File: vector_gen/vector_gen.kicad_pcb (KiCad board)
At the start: 2 copper layers, 91.4 x 101.6 mm, 99 parts, among them J1 ARDUINO POWER 3.3V, J10 ARDUINO J1, J11 Conn_01x08, J2 ARDUINO J3 3.3V, J3 ARDUINO J2 3.3V, J4 Conn_01x02_Female, J5 ARDUINO J1 3.3V, J6 Conn_01x03, J7 ARDUINO POWER, J8 ARDUINO J3, J9 ARDUINO J2, Q1 2N3904, U1 MCP4922, U10 MCP4922, U11 MCP4922, U12 4019, U13 LM336, U14 74HC86, U16 74LS07, U17 74LS07, U19 MAX4544, U5 4066, U6 MCP6292, U8 TL072IP, U9 LM319

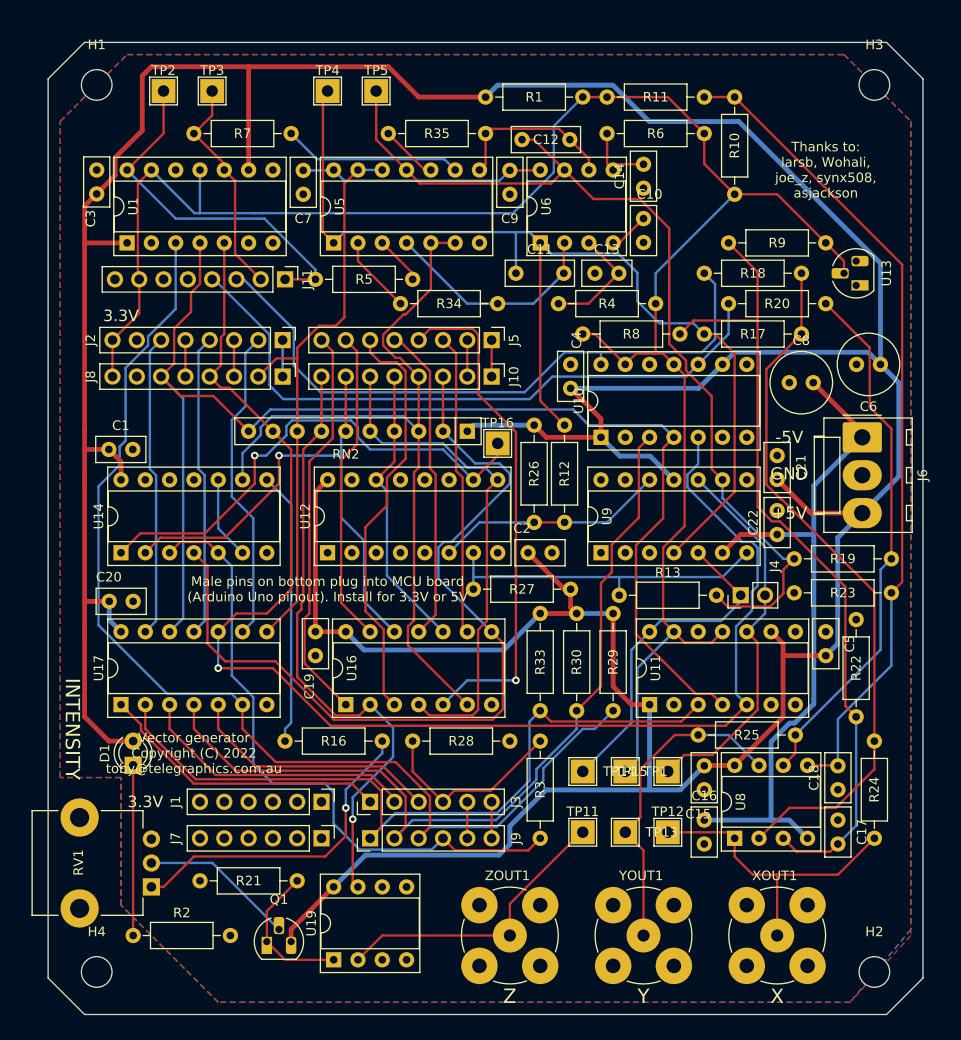
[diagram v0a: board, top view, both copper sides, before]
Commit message: Some important corrections. OSHpark candidate?
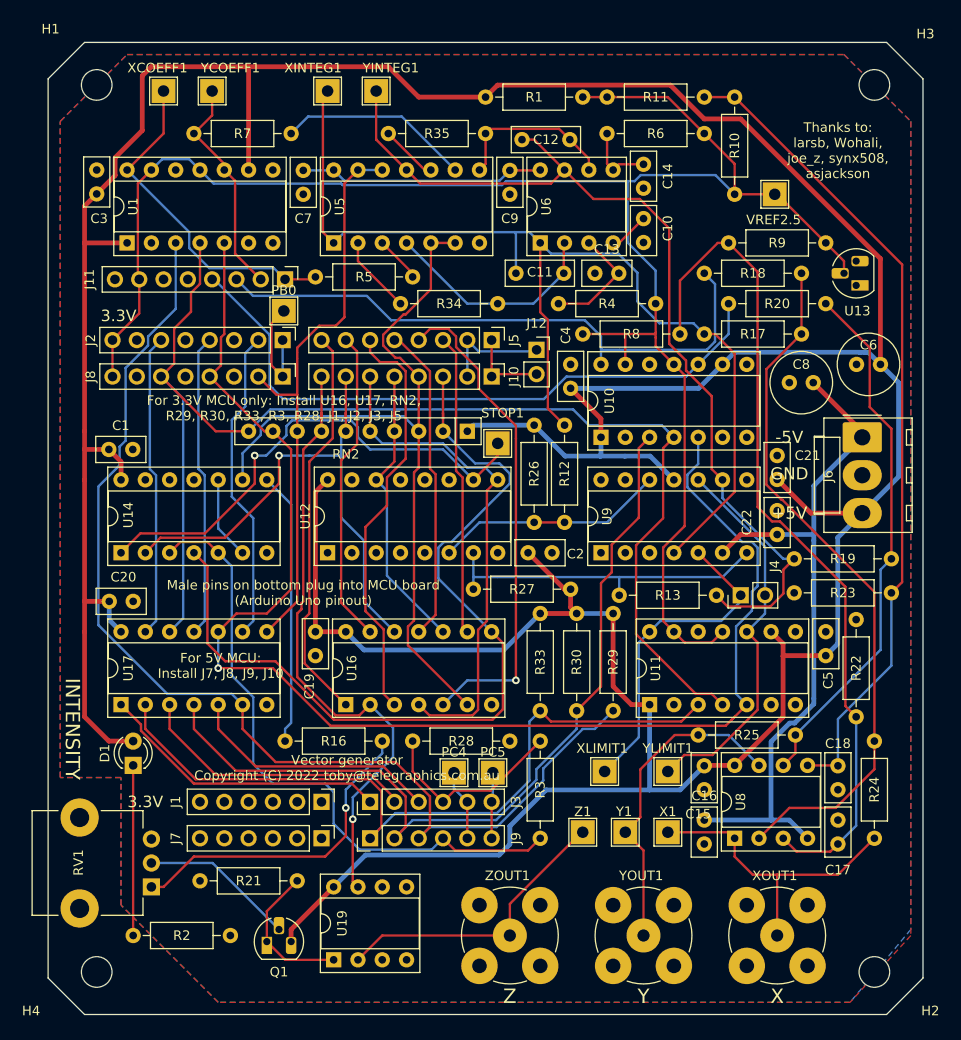
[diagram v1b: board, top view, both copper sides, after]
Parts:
- added J12: Conn_01x02, Connector_PinSocket_2.54mm:PinSocket_1x02_P2.54mm_Vertical, F.Cu at (-8.00, -24.4)
- added PB0: TestPoint, TestPoint:TestPoint_THTPad_2.5x2.5mm_Drill1.2mm, F.Cu at (-34.4, -28.4)
- added PC4: TestPoint, TestPoint:TestPoint_THTPad_2.5x2.5mm_Drill1.2mm, F.Cu at (-16.6, 19.8)
- added PC5: TestPoint, TestPoint:TestPoint_THTPad_2.5x2.5mm_Drill1.2mm, F.Cu at (-12.6, 19.8)
- moved VREF2.5 62.3 mm to (16.9, -40.6)
- moved XLIMIT1 2.29 mm to (-0.89, 19.7)
- moved R5 0.25 mm to (-21.0, -32.0)
- renumbered TP16 to STOP1, TP1 to VREF2.5, TP12 to X1, TP2 to XCOEFF1, TP4 to XINTEG1, TP14 to XLIMIT1, TP13 to Y1, TP3 to YCOEFF1, TP5 to YINTEG1, TP15 to YLIMIT1, TP11 to Z1
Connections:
- J1 pad 2: +3V3 -> GND
- J1 pad 3: Net-(J1-Pad3) -> GND
- J1 pad 4: GND -> Net-(J1-Pad4)
- J1 pad 5: GND -> +3V3
- J7 pad 2: Net-(J7-Pad2) -> GND
- J7 pad 3: Net-(J7-Pad3) -> GND
- J7 pad 4: GND -> Net-(J7-Pad4)
- J7 pad 5: GND -> Net-(J7-Pad5)
- J8 pad 1: Net-(J2-Pad1) -> Net-(J8-Pad1)
- J8 pad 3: Net-(J2-Pad3) -> Net-(J8-Pad3)
- J8 pad 5: Net-(J2-Pad5) -> Net-(J8-Pad5)
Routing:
- net Net-(J11-Pad7): track 204.7 -> 192.6 mm
- net Net-(J8-Pad1): track 0.00 -> 7.88 mm
- net Net-(J10-Pad2): track 3.81 -> 11.6 mm
- net Net-(J10-Pad1): track 3.81 -> 8.61 mm
- net Net-(J11-Pad3): track 68.0 -> 63.4 mm
- net Net-(J2-Pad5): track 3.81 -> 0.00 mm
- net Net-(J2-Pad3): track 3.81 -> 0.00 mm
- net Net-(J3-Pad5): track 3.81 -> 7.44 mm
- net Net-(C17-Pad2): track 84.9 -> 88.5 mm
- net Net-(J3-Pad6): track 3.81 -> 6.91 mm
- net Net-(J11-Pad1): track 38.0 -> 35.3 mm
- net +5V: track 467.7 -> 469.9 mm
- net Net-(J5-Pad4): track 53.4 -> 51.9 mm
- net Net-(R7-Pad1): track 18.7 -> 20.2 mm
- net Net-(J4-Pad1): track 35.3 -> 34.3 mm
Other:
- board text added: "For 3.3V MCU only: Install U16, U17, RN2, R29, R30, R33, R3, R28, J1, J2, J3, J5"
- board text added: "For 5V MCU: Install J7, J8, J9, J10"
- board text added: "Male pins on bottom plug into MCU board (Arduino Uno pinout)"
- board text removed: "Male pins on bottom plug into MCU board (Arduino Uno pinout). Install for 3.3V or 5V"

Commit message: New OSHPark manuf candidate.
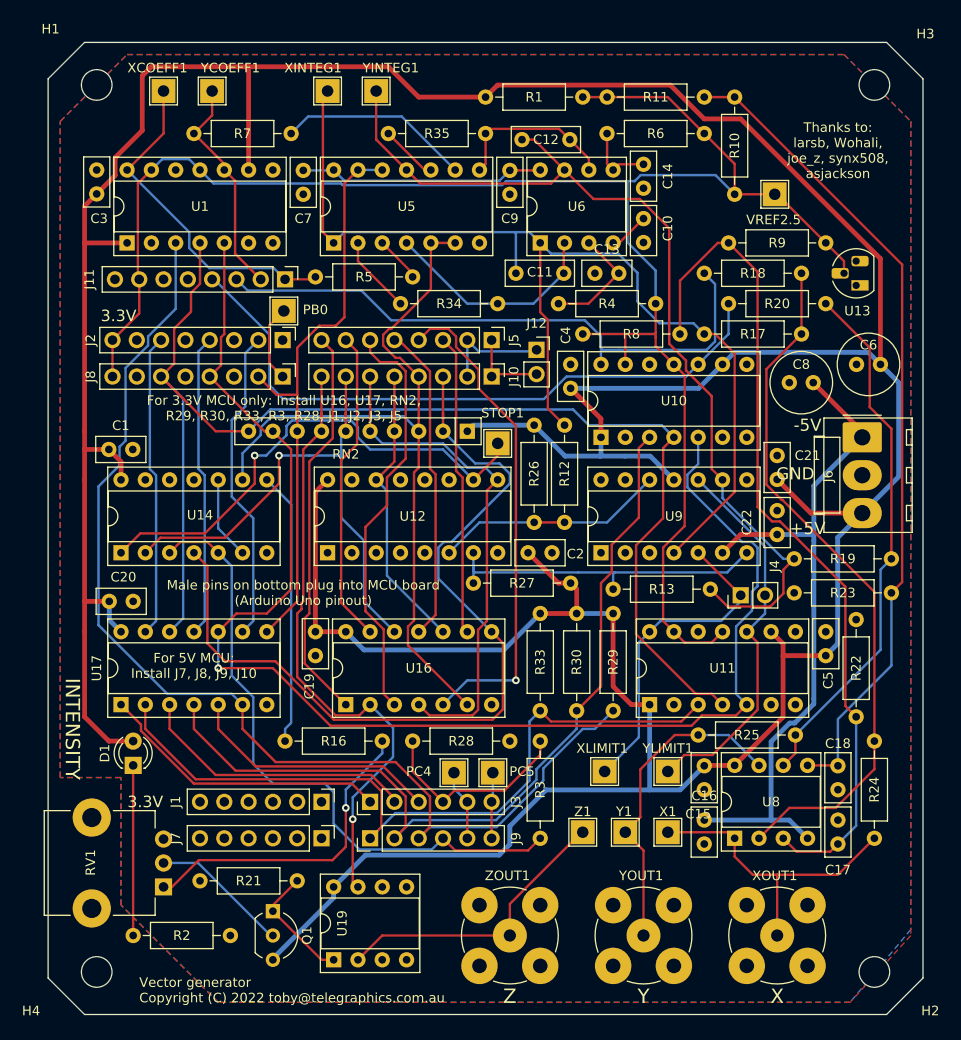
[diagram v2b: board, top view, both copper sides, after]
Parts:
- Q1: footprint Package_TO_SOT_THT:TO-92_HandSolder -> Package_TO_SOT_THT:TO-92_Inline_Wide
- moved Q1 3.24 mm to (-35.6, 34.3), turned to 270 degrees
- moved RV1 1.27 mm to (-47.0, 31.8)
- moved R13 0.90 mm to (0.00, 0.64)
- moved R27 0.64 mm to (-14.6, 0.00)
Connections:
- J8 pad 1: Net-(J8-Pad1) -> Net-(J2-Pad1)
- PB0 pad 1: Net-(J8-Pad1) -> Net-(J2-Pad1)
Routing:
- net Net-(J8-Pad1): track 7.88 -> 0.00 mm
- net Net-(J2-Pad1): track 3.81 -> 8.04 mm
- net +5V: track 469.9 -> 473.0 mm
- net Net-(Q1-Pad1): track 15.4 -> 12.7 mm
- net Net-(Q1-Pad2): track 16.2 -> 14.6 mm
- net Net-(C12-Pad1): track 99.2 -> 100.1 mm
- net Net-(J3-Pad4): track 20.5 -> 21.3 mm
- net Net-(R16-Pad2): track 34.0 -> 33.4 mm

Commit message: New OSHPark manuf candidate.
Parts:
- C6, C8: footprint Capacitor_THT:C_Radial_D6.3mm_H7.0mm_P2.50mm -> Capacitor_THT:CP_Radial_D6.3mm_P2.50mm
- moved C8 2.62 mm to (21.0, -20.3), turned to 180 degrees
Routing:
- net -5V: track 74.0 -> 75.9 mm
- net Net-(J2-Pad1): track 8.04 -> 9.52 mm

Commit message: New manuf candidate.
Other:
- rule pad_to_mask_clearance: 0.0508 -> 0
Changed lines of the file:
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@@
     (thickness 1.6)
     (drawings 28)
-    (tracks 787)
+    (tracks 785)
     (zones 0)
     (modules 103)
@@
     (pad_size 1.524 1.524)
     (pad_drill 0.762)
-    (pad_to_mask_clearance 0.0508)
+    (pad_to_mask_clearance 0)
     (aux_axis_origin 0 0)
     (grid_origin -52.705 -35.56)
     (visible_elements FFFFFF7F)
     (pcbplotparams
-      (layerselection 0x010fc_ffffffff)
-      (usegerberextensions false)
-      (usegerberattributes true)
-      (usegerberadvancedattributes true)
-      (creategerberjobfile true)
+      (layerselection 0x010f0_ffffffff)
+      (usegerberextensions true)
+      (usegerberattributes false)
+      (usegerberadvancedattributes false)
+      (creategerberjobfile false)
       (excludeedgelayer true)
       (linewidth 0.100000)
@@
       (psa4output false)
       (plotreference true)
-      (plotvalue true)
+      (plotvalue false)
       (plotinvisibletext false)
       (padsonsilk false)
-      (subtractmaskfromsilk false)
+      (subtractmaskfromsilk true)
       (outputformat 1)
       (mirror false)
-      (drillshape 1)
+      (drillshape 0)
       (scaleselection 1)
-      (outputdirectory ""))
+      (outputdirectory "jlpcb_gerbers"))
   )
   (net 0 "")
@@
       (effects (font (size 1 1) (thickness 0.15)))
     )
-    (fp_text user %R (at 1.25 0) (layer F.Fab)
-      (effects (font (size 1 1) (thickness 0.15)))
-    )
     (fp_circle (center 1.25 0) (end 4.4 0) (layer F.Fab) (width 0.1))
     (fp_circle (center 1.25 0) (end 4.52 0) (layer F.SilkS) (width 0.12))
@@
     (fp_line (start -2.250241 -1.839) (end -1.620241 -1.839) (layer F.SilkS) (width 0.12))
     (fp_line (start -1.935241 -2.154) (end -1.935241 -1.524) (layer F.SilkS) (width 0.12))
+    (fp_text user %R (at 1.25 0) (layer F.Fab)
+      (effects (font (size 1 1) (thickness 0.15)))
+    )
     (pad 2 thru_hole circle (at 2.5 0 180) (size 1.6 1.6) (drill 0.8) (layers *.Cu *.Mask)
       (net 27 -5V))
@@
       (effects (font (size 1 1) (thickness 0.15)))
     )
-    (fp_text user %R (at 1.25 0) (layer F.Fab)
-      (effects (font (size 1 1) (thickness 0.15)))
-    )
     (fp_circle (center 1.25 0) (end 4.4 0) (layer F.Fab) (width 0.1))
     (fp_circle (center 1.25 0) (end 4.52 0) (layer F.SilkS) (width 0.12))
@@
     (fp_line (start -2.250241 -1.839) (end -1.620241 -1.839) (layer F.SilkS) (width 0.12))
     (fp_line (start -1.935241 -2.154) (end -1.935241 -1.524) (layer F.SilkS) (width 0.12))
+    (fp_text user %R (at 1.25 0) (layer F.Fab)
+      (effects (font (size 1 1) (thickness 0.15)))
+    )
     (pad 2 thru_hole circle (at 2.5 0 180) (size 1.6 1.6) (drill 0.8) (layers *.Cu *.Mask)
       (net 2 GND))
@@
     (pad 2 thru_hole oval (at 3.96 0 270) (size 3.16 4.1) (drill 1.7) (layers *.Cu *.Mask)
       (net 2 GND))
-    (pad 1 thru_hole roundrect (at 0 0 270) (size 3.16 4.1) (drill 1.7) (layers *.Cu *.Mask) (roundrect_rratio 0.079114)
+    (pad 1 thru_hole roundrect (at 0 0 270) (size 3.16 4.1) (drill 1.7) (layers *.Cu *.Mask) (roundrect_rratio 0.07911392405063292)
       (net 27 -5V))
     (model ${KISYS3DMOD}/Connector_Molex.3dshapes/Molex_KK-396_A-41791-0003_1x03_P3.96mm_Vertical.wrl
@@
   (segment (start -27.214999 24.674999) (end -27.214999 31.205001) (width 0.25) (layer F.Cu) (net 37))
   (segment (start -26.525001 13.825001) (end -25.4 12.7) (width 0.25) (layer F.Cu) (net 37))
-  (segment (start -32.56999 2.72499) (end -33.02 3.175) (width 0.25) (layer F.Cu) (net 37))
-  (segment (start -32.385 1.905) (end -32.56999 2.08999) (width 0.25) (layer F.Cu) (net 37))
-  (segment (start -32.385 -13.97) (end -32.385 1.905) (width 0.25) (layer F.Cu) (net 37))
-  (segment (start -33.02 9.805002) (end -29.000001 13.825001) (width 0.25) (layer F.Cu) (net 37))
-  (segment (start -32.56999 2.08999) (end -32.56999 2.72499) (width 0.25) (layer F.Cu) (net 37))
+  (segment (start -33.02 3.80859) (end -33.02 9.805002) (width 0.25) (layer F.Cu) (net 37))
   (segment (start -29.000001 13.825001) (end -26.525001 13.825001) (width 0.25) (layer F.Cu) (net 37))
-  (segment (start -33.02 3.175) (end -33.02 9.805002) (width 0.25) (layer F.Cu) (net 37))
+  (segment (start -32.385 3.17359) (end -33.02 3.80859) (width 0.25) (layer F.Cu) (net 37))
+  (segment (start -33.02 9.805002) (end -29.000001 13.825001) (width 0.25) (layer F.Cu) (net 37))
+  (segment (start -32.385 -13.97) (end -32.385 3.17359) (width 0.25) (layer F.Cu) (net 37))
   (segment (start -30.48 -15.875) (end -32.385 -13.97) (width 0.25) (layer F.Cu) (net 37))
   (segment (start -27.94 -15.875) (end -27.94 -17.78) (width 0.25) (layer F.Cu) (net 38))

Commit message: New manuf candidate.
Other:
- board text added: "3.3 V >"
- board text added: "3.3V >"
- board text added: "5V"
- board text added: "In memory of bootnecklad 1995 – 2018"
- board text removed: "In memory of bootnecklad 1995–2018"
